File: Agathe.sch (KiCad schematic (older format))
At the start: 185 parts, among them J1 Conn_01x04_Female, J2 Conn_01x04_Female, J3 AVR-ISP-6, SW1 SW_Push, U1 ATmega32U4-AU, U2 PRTR5V0U2X, Y1 16MHz

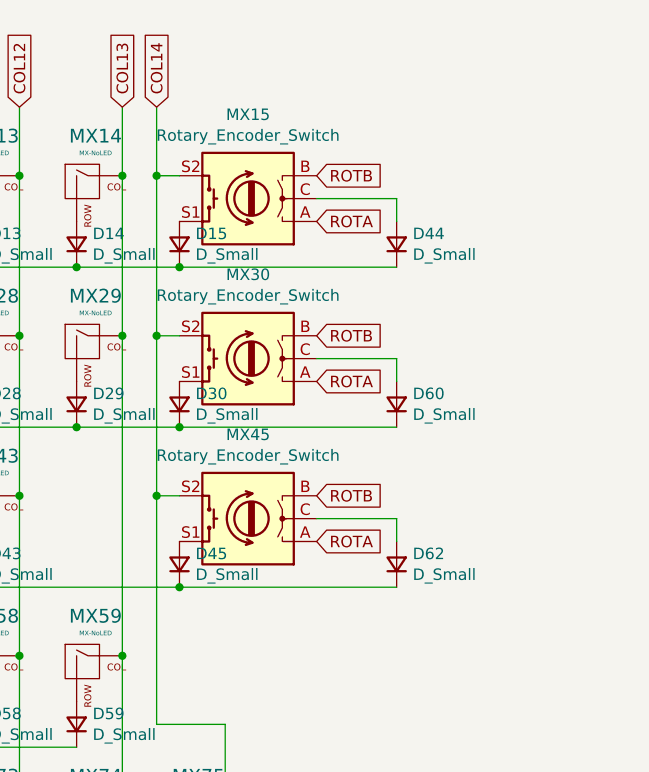
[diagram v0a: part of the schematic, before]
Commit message: add matrice rotary possibilities
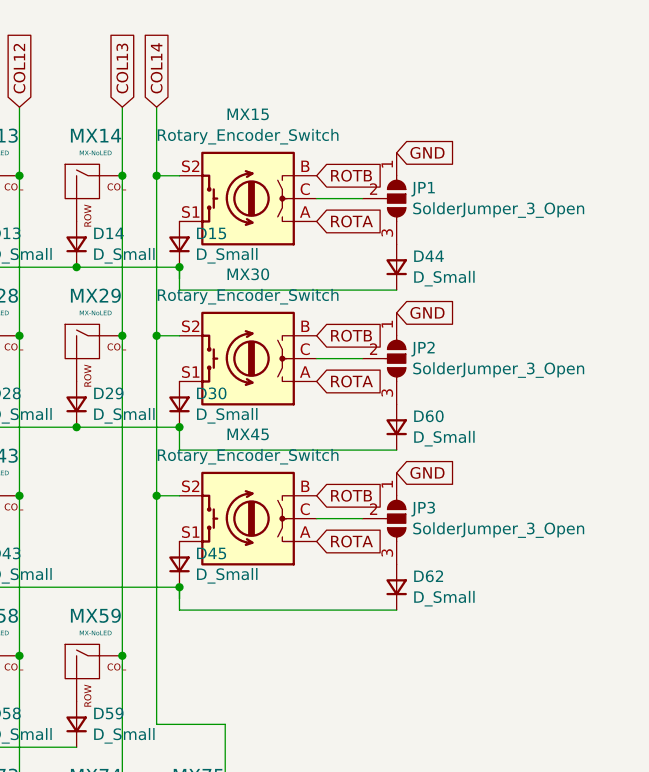
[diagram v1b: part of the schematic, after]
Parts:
- added JP1, JP2, JP3: SolderJumper_3_Open, Jumper:SolderJumper-3_P1.3mm_Open_Pad1.0x1.5mm_NumberLabels, symbol Jumper:SolderJumper_3_Open
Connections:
- net GND: now also JP1.1 (A), JP2.1 (A), JP3.1 (A)
- net at MX15.C: now also JP1.2 (C); no longer D44.2 (A)
- net at MX30.C: now also JP2.2 (C); no longer D60.2 (A)
- net at MX45.C: now also JP3.2 (C); no longer D62.2 (A)
- new net: D44.2 (A), JP1.3 (B)
- new net: D60.2 (A), JP2.3 (B)
- new net: D62.2 (A), JP3.3 (B)
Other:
- moved on the sheet: D44, D60, D62
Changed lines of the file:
@@
 L Device:D_Small D62
 U 1 1 603BD856
-P 14700 2800
-F 0 "D62" V 14746 2730 50  0000 R CNN
-F 1 "D_Small" V 14655 2730 50  0000 R CNN
-F 2 "Diode_SMD:D_SOD-123" V 14700 2800 50  0001 C CNN
-F 3 "~" V 14700 2800 50  0001 C CNN
-	1    14700 2800
+P 14700 2900
+F 0 "D62" V 14746 2830 50  0000 R CNN
+F 1 "D_Small" V 14655 2830 50  0000 R CNN
+F 2 "Diode_SMD:D_SOD-123" V 14700 2900 50  0001 C CNN
+F 3 "~" V 14700 2900 50  0001 C CNN
+	1    14700 2900
 	0    -1   -1   0
 $EndComp
-Wire Wire Line
-	14350 2600 14700 2600
-Wire Wire Line
-	14700 2600 14700 2700
-Wire Wire Line
-	14700 2900 13750 2900
 Connection ~ 13750 2900
 $Comp
 L Device:D_Small D60
 U 1 1 603F9CA7
-P 14700 2100
-F 0 "D60" V 14746 2030 50  0000 R CNN
-F 1 "D_Small" V 14655 2030 50  0000 R CNN
-F 2 "Diode_SMD:D_SOD-123" V 14700 2100 50  0001 C CNN
-F 3 "~" V 14700 2100 50  0001 C CNN
-	1    14700 2100
+P 14700 2200
+F 0 "D60" V 14746 2130 50  0000 R CNN
+F 1 "D_Small" V 14655 2130 50  0000 R CNN
+F 2 "Diode_SMD:D_SOD-123" V 14700 2200 50  0001 C CNN
+F 3 "~" V 14700 2200 50  0001 C CNN
+	1    14700 2200
 	0    -1   -1   0
 $EndComp
@@
 L Device:D_Small D44
 U 1 1 603FA36B
-P 14700 1400
-F 0 "D44" V 14746 1330 50  0000 R CNN
-F 1 "D_Small" V 14655 1330 50  0000 R CNN
-F 2 "Diode_SMD:D_SOD-123" V 14700 1400 50  0001 C CNN
-F 3 "~" V 14700 1400 50  0001 C CNN
-	1    14700 1400
+P 14700 1500
+F 0 "D44" V 14746 1430 50  0000 R CNN
+F 1 "D_Small" V 14655 1430 50  0000 R CNN
+F 2 "Diode_SMD:D_SOD-123" V 14700 1500 50  0001 C CNN
+F 3 "~" V 14700 1500 50  0001 C CNN
+	1    14700 1500
 	0    -1   -1   0
 $EndComp
+Text GLabel 14700 1000 2    50   Input ~ 0
+GND
+$Comp
+L Jumper:SolderJumper_3_Open JP1
+U 1 1 5F9D8F7D
+P 14700 1200
+F 0 "JP1" V 14654 1268 50  0000 L CNN
+F 1 "SolderJumper_3_Open" V 14745 1268 50  0000 L CNN
+F 2 "Jumper:SolderJumper-3_P1.3mm_Open_Pad1.0x1.5mm_NumberLabels" H 14700 1200 50  0001 C CNN
+F 3 "~" H 14700 1200 50  0001 C CNN
+	1    14700 1200
+	0    1    1    0
+$EndComp
+$Comp
+L Jumper:SolderJumper_3_Open JP2
+U 1 1 5F9D9785
+P 14700 1900
+F 0 "JP2" V 14654 1968 50  0000 L CNN
+F 1 "SolderJumper_3_Open" V 14745 1968 50  0000 L CNN
+F 2 "Jumper:SolderJumper-3_P1.3mm_Open_Pad1.0x1.5mm_NumberLabels" H 14700 1900 50  0001 C CNN
+F 3 "~" H 14700 1900 50  0001 C CNN
+	1    14700 1900
+	0    1    1    0
+$EndComp
+$Comp
+L Jumper:SolderJumper_3_Open JP3
+U 1 1 5F9D9D5F
+P 14700 2600
+F 0 "JP3" V 14654 2668 50  0000 L CNN
+F 1 "SolderJumper_3_Open" V 14745 2668 50  0000 L CNN
+F 2 "Jumper:SolderJumper-3_P1.3mm_Open_Pad1.0x1.5mm_NumberLabels" H 14700 2600 50  0001 C CNN
+F 3 "~" H 14700 2600 50  0001 C CNN
+	1    14700 2600
+	0    1    1    0
+$EndComp
+Connection ~ 13750 2200
+Text GLabel 14700 2400 2    50   Input ~ 0
+GND
+Connection ~ 13750 1500
+Text GLabel 14700 1700 2    50   Input ~ 0
+GND
 Wire Wire Line
-	13750 2200 14700 2200
-Connection ~ 13750 2200
+	14350 2600 14550 2600
 Wire Wire Line
-	14700 2000 14700 1900
+	14700 3000 13750 3000
 Wire Wire Line
-	14700 1900 14350 1900
+	13750 2950 13750 2900
 Wire Wire Line
-	14350 1200 14700 1200
+	13750 2900 13750 3000
 Wire Wire Line
-	14700 1200 14700 1300
+	14350 1900 14550 1900
 Wire Wire Line
-	14700 1500 13750 1500
-Connection ~ 13750 1500
+	14700 2300 13750 2300
+Wire Wire Line
+	13750 2200 13750 2300
+Wire Wire Line
+	14700 1600 13750 1600
+Wire Wire Line
+	13750 1550 13750 1500
+Wire Wire Line
+	13750 1500 13750 1600
+Wire Wire Line
+	14350 1200 14550 1200
 $EndSCHEMATC

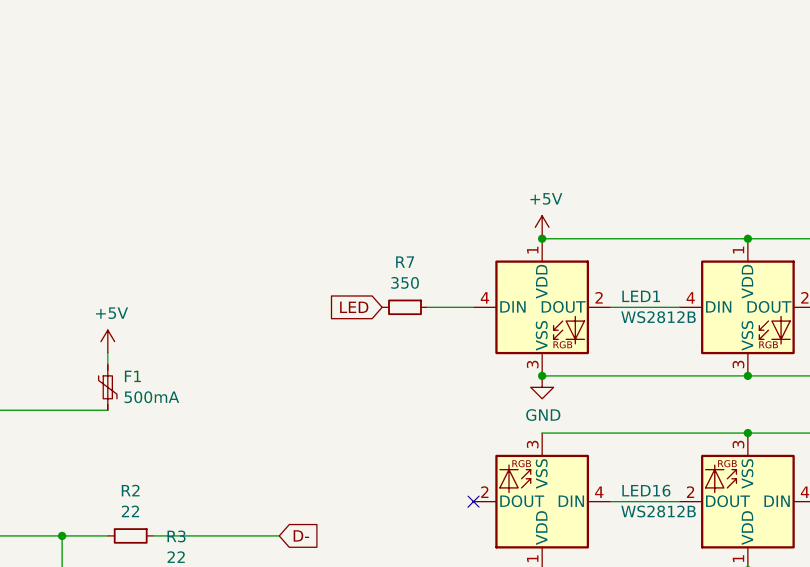
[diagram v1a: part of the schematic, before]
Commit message: move the daughterboard at the bottom and change the mcu
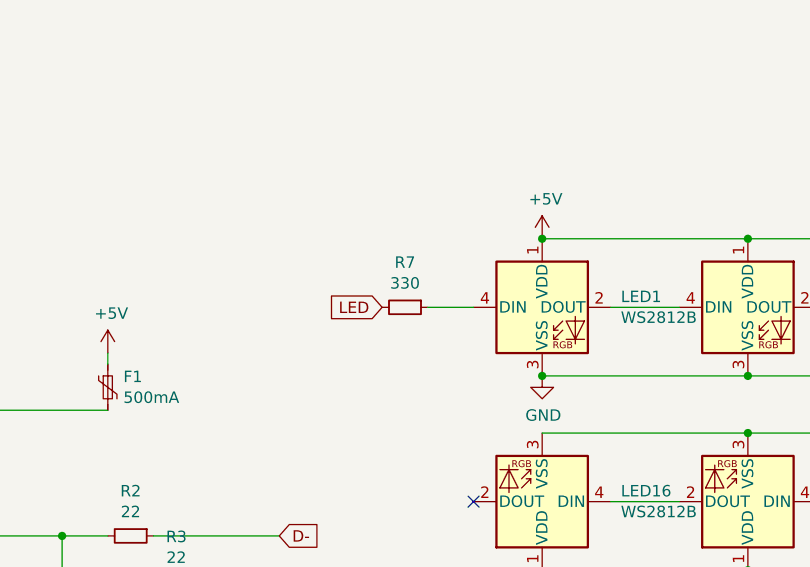
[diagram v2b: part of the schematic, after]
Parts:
- R7: value 350 -> 330
- U1: footprint Keebio-Parts:ATMEGA32U4-AU -> Package_DFN_QFN:QFN-44-1EP_7x7mm_P0.5mm_EP5.2x5.2mm
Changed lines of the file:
@@
 F 0 "U1" H 1950 811 50  0000 C CNN
 F 1 "ATmega32U4-AU" H 1950 720 50  0000 C CNN
-F 2 "Keebio-Parts:ATMEGA32U4-AU" H 1950 2700 50  0001 C CIN
+F 2 "Package_DFN_QFN:QFN-44-1EP_7x7mm_P0.5mm_EP5.2x5.2mm" H 1950 2700 50  0001 C CIN
 F 3 "http://ww1.microchip.com/downloads/en/DeviceDoc/Atmel-7766-8-bit-AVR-ATmega16U4-32U4_Datasheet.pdf" H 1950 2700 50  0001 C CNN
 	1    1950 2700
@@
 P 4800 5000
 F 0 "R7" V 4604 5000 50  0000 C CNN
-F 1 "350" V 4695 5000 50  0000 C CNN
+F 1 "330" V 4695 5000 50  0000 C CNN
 F 2 "Resistor_SMD:R_0805_2012Metric" H 4800 5000 50  0001 C CNN
 F 3 "~" H 4800 5000 50  0001 C CNN

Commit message: replace the mcu by an elite-c in the schema
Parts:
- removed C1: 1uF, Capacitor_SMD:C_0805_2012Metric, symbol Device:C_Small
- removed C2, C3, C4, C8: 0.1uF, Capacitor_SMD:C_0805_2012Metric, symbol Device:C_Small
- removed C5: 10uF, Capacitor_SMD:C_0805_2012Metric, symbol Device:C_Small
- removed C6, C7: 22pF, Capacitor_SMD:C_0805_2012Metric, symbol Device:C_Small
- removed F1: 500mA, Fuse:Fuse_1206_3216Metric, symbol Device:Polyfuse_Small
- removed FB1, FB2: Ferrite_Bead_Small, Inductor_SMD:L_0805_2012Metric_Pad1.15x1.40mm_HandSolder, symbol Device:Ferrite_Bead_Small
- removed J1, J2: Conn_01x04_Female, Connector_PinHeader_2.54mm:PinHeader_1x04_P2.54mm_Vertical, symbol Connector:Conn_01x04_Female
- removed J3: AVR-ISP-6, random-keyboard-parts:Reset_Pretty-Mask, symbol Connector:AVR-ISP-6
- removed R1, R4: 10k, Resistor_SMD:R_0805_2012Metric, symbol Device:R_Small
- removed R2, R3: 22, Resistor_SMD:R_0805_2012Metric, symbol Device:R_Small
- removed R5, R6, R8, R9: 5.1k, Resistor_SMD:R_0805_2012Metric, symbol Device:R_Small
- removed SW1: SW_Push, random-keyboard-parts:SKQG-1155865, symbol Switch:SW_Push
- removed U1: ATmega32U4-AU, Package_DFN_QFN:QFN-44-1EP_7x7mm_P0.5mm_EP5.2x5.2mm, symbol MCU_Microchip_ATmega:ATmega32U4-AU
- removed U2: PRTR5V0U2X, random-keyboard-parts:SOT143B, symbol Power_Protection:PRTR5V0U2X
- removed USB1, USB2: USB_C_Receptacle_USB2.0, Connector_USB:USB_C_Receptacle_HRO_TYPE-C-31-M-12, symbol Connector:USB_C_Receptacle_USB2.0
- removed Y1: 16MHz, Crystal:Crystal_SMD_3225-4Pin_3.2x2.5mm, symbol Device:Crystal_GND24_Small
- added U1: Elite-C, Keebio-Parts:Elite-C, symbol lckprt:Elite-C
- D1, D10, D11, D12, D13, D14, D15, D16, D17, D18, D19, D2, D20, D21, D22, D23, D24, D25, D26, D27, D28, D29, D3, D30, D31, D32, D33, D34, D35, D36, D37, D38, D39, D4, D40, D41, D42, D43, D44, D45, D46, D47, D48, D49, D5, D50, D51, D52, D53, D54, D55, D56, D57, D58, D59, D6, D60, D61, D62, D63, D65, D66, D68, D7, D70, D73, D74, D75, D8, D9: footprint Diode_SMD:D_SOD-123 -> Keebio-Parts:Diode-Hybrid-Back
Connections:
- net +5V: now also U1.21 (VCC)
- net COL0: now also U1.12 (B5)
- net COL1: now also U1.13 (B6)
- net COL10: now also U1.26 (D5)
- net COL11: now also U1.27 (C7)
- net COL12: now also U1.24 (B0)
- net COL13: now also U1.28 (F1)
- net COL14: now also U1.29 (F0)
- net COL2: now also U1.14 (B2)
- net COL3: now also U1.15 (B3)
- net COL4: now also U1.16 (B1)
- net COL5: now also U1.17 (F7)
- net COL6: now also U1.18 (F6)
- net COL7: now also U1.19 (F5)
- net COL8: now also U1.20 (F4)
- net COL9: now also U1.25 (B7)
- net GND: now also U1.23 (GND), U1.3 (GND), U1.4 (GND)
- net LED: now also U1.1 (D3)
- net ROTB: now also U1.6 (SCL)
- net ROW0: now also U1.7 (D4)
- net ROW1: now also U1.8 (C6)
- net ROW2: now also U1.9 (D7)
- net ROW3: now also U1.10 (E6)
- net ROW4: now also U1.11 (B4)
- net MISO renamed ROTA
- net ROTA: now also U1.5 (SDA)
- no-connect marks 6 -> 3
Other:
- moved on the sheet: C10, C11, C9, D1, D10, D11, D12, D13, D14, D15, D16, D17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

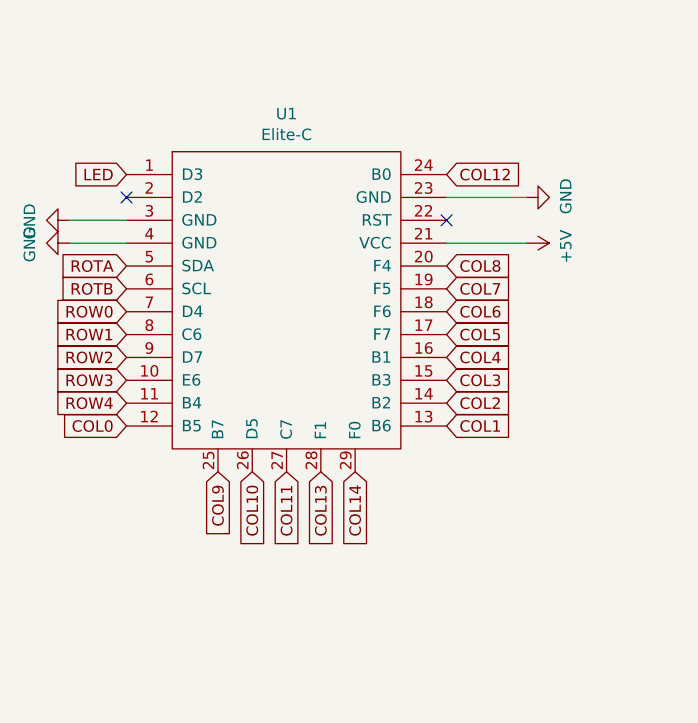
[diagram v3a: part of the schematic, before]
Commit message: pcb adapted for elite-c and th diodes
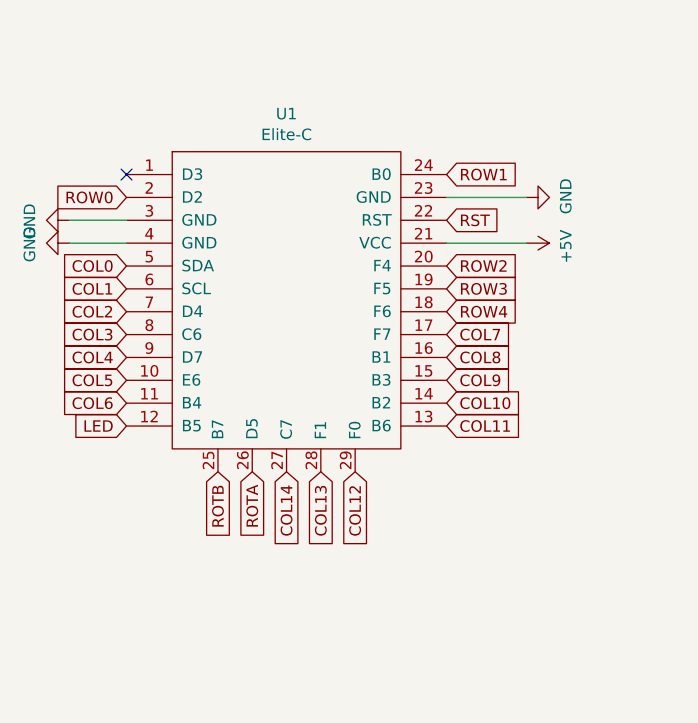
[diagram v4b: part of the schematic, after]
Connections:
- net COL0: now also U1.5 (SDA); no longer U1.12 (B5)
- net COL1: now also U1.6 (SCL); no longer U1.13 (B6)
- net COL10: now also U1.14 (B2); no longer U1.26 (D5)
- net COL11: now also U1.13 (B6); no longer U1.27 (C7)
- net COL12: now also U1.29 (F0); no longer U1.24 (B0)
- net COL14: now also U1.27 (C7); no longer U1.29 (F0)
- net COL2: now also U1.7 (D4); no longer U1.14 (B2)
- net COL3: now also U1.8 (C6); no longer U1.15 (B3)
- net COL4: now also U1.9 (D7); no longer U1.16 (B1)
- net COL5: now also U1.10 (E6); no longer U1.17 (F7)
- net COL6: now also U1.11 (B4); no longer U1.18 (F6)
- net COL7: now also U1.17 (F7); no longer U1.19 (F5)
- net COL8: now also U1.16 (B1); no longer U1.20 (F4)
- net COL9: now also U1.15 (B3); no longer U1.25 (B7)
- net LED: now also U1.12 (B5); no longer U1.1 (D3)
- net ROTA: now also U1.26 (D5); no longer U1.5 (SDA)
- net ROTB: now also U1.25 (B7); no longer U1.6 (SCL)
- net ROW0: now also U1.2 (D2); no longer U1.7 (D4)
- net ROW1: now also U1.24 (B0); no longer U1.8 (C6)
- net ROW2: now also U1.20 (F4); no longer U1.9 (D7)
- net ROW3: now also U1.19 (F5); no longer U1.10 (E6)
- net ROW4: now also U1.18 (F6); no longer U1.11 (B4)
- net RST: now reaches U1.22 (RST)
- no-connect marks 3 -> 2
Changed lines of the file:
@@
 	1    0    0    -1
 $EndComp
+Text GLabel 1300 1450 0    50   Input ~ 0
+ROW0
+Text GLabel 2700 1350 2    50   Input ~ 0
+ROW1
+Text GLabel 2700 1750 2    50   Input ~ 0
+ROW2
+Text GLabel 2700 1850 2    50   Input ~ 0
+ROW3
+Text GLabel 2700 1950 2    50   Input ~ 0
+ROW4
+Text GLabel 1300 1750 0    50   Input ~ 0
+COL0
+Text GLabel 1300 1850 0    50   Input ~ 0
+COL1
 Text GLabel 1300 1950 0    50   Input ~ 0
-ROW0
+COL2
 Text GLabel 1300 2050 0    50   Input ~ 0
-ROW1
+COL3
 Text GLabel 1300 2150 0    50   Input ~ 0
-ROW2
+COL4
 Text GLabel 1300 2250 0    50   Input ~ 0
-ROW3
+COL5
 Text GLabel 1300 2350 0    50   Input ~ 0
-ROW4
-Text GLabel 1300 2450 0    50   Input ~ 0
-COL0
+COL6
+Text GLabel 2700 2050 2    50   Input ~ 0
+COL7
+Text GLabel 2700 2150 2    50   Input ~ 0
+COL8
+Text GLabel 2700 2250 2    50   Input ~ 0
+COL9
+Text GLabel 2700 2350 2    50   Input ~ 0
+COL10
 Text GLabel 2700 2450 2    50   Input ~ 0
-COL1
-Text GLabel 2700 2350 2    50   Input ~ 0
-COL2
-Text GLabel 2700 2250 2    50   Input ~ 0
-COL3
-Text GLabel 2700 2150 2    50   Input ~ 0
-COL4
-Text GLabel 2700 2050 2    50   Input ~ 0
-COL5
-Text GLabel 2700 1950 2    50   Input ~ 0
-COL6
-Text GLabel 2700 1850 2    50   Input ~ 0
-COL7
-Text GLabel 2700 1750 2    50   Input ~ 0
-COL8
-Text GLabel 1700 2650 3    50   Input ~ 0
-COL9
-Text GLabel 1850 2650 3    50   Input ~ 0
-COL10
-Text GLabel 2000 2650 3    50   Input ~ 0
 COL11
-Text GLabel 2700 1350 2    50   Input ~ 0
+Text GLabel 2300 2650 3    50   Input ~ 0
 COL12
 Text GLabel 2150 2650 3    50   Input ~ 0
 COL13
-Text GLabel 2300 2650 3    50   Input ~ 0
+Text GLabel 2000 2650 3    50   Input ~ 0
 COL14
-Text GLabel 1300 1350 0    50   Input ~ 0
+Text GLabel 1300 2450 0    50   Input ~ 0
 LED
-Text GLabel 1300 1850 0    50   Input ~ 0
+Text GLabel 1700 2650 3    50   Input ~ 0
 ROTB
-Text GLabel 1300 1750 0    50   Input ~ 0
+Text GLabel 1850 2650 3    50   Input ~ 0
 ROTA
 Wire Wire Line
@@
 Wire Wire Line
 	1050 1650 1300 1650
-NoConn ~ 2700 1550
-NoConn ~ 1300 1450
+Text GLabel 2700 1550 2    50   Input ~ 0
+RST
+NoConn ~ 1300 1350
 $EndSCHEMATC

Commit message: elite-c horizontal
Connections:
- net LED: now also U1.1 (D3); no longer U1.12 (B5)
- net ROW0: now also U1.12 (B5); no longer U1.2 (D2)
- no-connect marks 2 -> 1
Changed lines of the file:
@@
 	1    0    0    -1
 $EndComp
-Text GLabel 1300 1450 0    50   Input ~ 0
+Text GLabel 1300 2450 0    50   Input ~ 0
 ROW0
 Text GLabel 2700 1350 2    50   Input ~ 0
@@
 Text GLabel 2000 2650 3    50   Input ~ 0
 COL14
-Text GLabel 1300 2450 0    50   Input ~ 0
+Text GLabel 1300 1350 0    50   Input ~ 0
 LED
 Text GLabel 1700 2650 3    50   Input ~ 0
@@
 Text GLabel 2700 1550 2    50   Input ~ 0
 RST
-NoConn ~ 1300 1350
 $EndSCHEMATC
